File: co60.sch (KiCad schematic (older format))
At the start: 23 parts, among them J1 Conn_01x06, Q1 PZT2222A, SW1 SW_Push, U1 ATMEGA32U4, Y1 16MHz

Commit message: Add: Part numbers to top level schematic
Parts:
- C1, C2: Product (none) -> 06035A220JAT2A
- C3, C8: Product (none) -> CGB3B3JB1C105K055AB
- C4, C5, C6, C7: Product (none) -> C1608X8R1E104K080AA
- F1: Product (none) -> 0805L050WR
- RC1: Product (none) -> RC0603JR-071K5L
- R_MCU_3, R_MCU_4: Product (none) -> ERJ-3GEYJ103V
- R_USB_1, R_USB_2: Product (none) -> RC0603JR-0722RL
- R_USB_3, R_USB_4: Product (none) -> RMCF0603JT5K10
- SW1: DigiKey Page (none) -> https://www.digikey.ca/product-detail/en/e-switch/TL3342F16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; Product (none) -> TL3342F160QG/TR
- Y1: Product (none) -> NX2520SA-16MHZ-STD-CSW-4
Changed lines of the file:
@@
 F 1 "22p" H 7030 3280 30  0000 L CNN
 F 2 "Capacitors_SMD:C_0603" H 7043 3230 50  0001 C CNN
-F 3 "" H 7005 3380 50  0001 C CNN
+F 3 "http://datasheets.avx.com/C0GNP0-Dielectric.pdf" H 7005 3380 50  0001 C CNN
+F 4 "06035A220JAT2A" H 7005 3380 60  0001 C CNN "Product"
 	1    7005 3380
 	1    0    0    -1
@@
 F 1 "22p" H 6480 3280 30  0000 L CNN
 F 2 "Capacitors_SMD:C_0603" H 6493 3230 50  0001 C CNN
-F 3 "" H 6455 3380 50  0001 C CNN
+F 3 "http://datasheets.avx.com/C0GNP0-Dielectric.pdf" H 6455 3380 50  0001 C CNN
+F 4 "06035A220JAT2A" H 6455 3380 60  0001 C CNN "Product"
 	1    6455 3380
 	1    0    0    -1
@@
 F 1 "1u" H 6700 5605 50  0000 L CNN
 F 2 "Capacitors_SMD:C_0603" H 6713 5555 50  0001 C CNN
-F 3 "" H 6675 5705 50  0001 C CNN
+F 3 "https://product.tdk.com/info/en/catalog/datasheets/mlcc_commercial_lowprofile_en.pdf" H 6675 5705 50  0001 C CNN
+F 4 "CGB3B3JB1C105K055AB" H 6675 5705 60  0001 C CNN "Product"
 	1    6675 5705
 	1    0    0    -1
@@
 F 1 "100n" H 1175 950 50  0000 L CNN
 F 2 "Capacitors_SMD:C_0603" H 1188 900 50  0001 C CNN
-F 3 "" H 1150 1050 50  0001 C CNN
+F 3 "https://product.tdk.com/info/en/catalog/datasheets/mlcc_commercial_hightemp_en.pdf" H 1150 1050 50  0001 C CNN
+F 4 "C1608X8R1E104K080AA" H 1150 1050 60  0001 C CNN "Product"
 	1    1150 1050
 	1    0    0    -1
@@
 F 1 "100n" H 1425 950 50  0000 L CNN
 F 2 "Capacitors_SMD:C_0603" H 1438 900 50  0001 C CNN
-F 3 "" H 1400 1050 50  0001 C CNN
+F 3 "https://product.tdk.com/info/en/catalog/datasheets/mlcc_commercial_hightemp_en.pdf" H 1400 1050 50  0001 C CNN
+F 4 "C1608X8R1E104K080AA" H 1400 1050 60  0001 C CNN "Product"
 	1    1400 1050
 	1    0    0    -1
@@
 F 1 "100n" H 1675 950 50  0000 L CNN
 F 2 "Capacitors_SMD:C_0603" H 1688 900 50  0001 C CNN
-F 3 "" H 1650 1050 50  0001 C CNN
+F 3 "https://product.tdk.com/info/en/catalog/datasheets/mlcc_commercial_hightemp_en.pdf" H 1650 1050 50  0001 C CNN
+F 4 "C1608X8R1E104K080AA" H 1650 1050 60  0001 C CNN "Product"
 	1    1650 1050
 	1    0    0    -1
@@
 F 1 "100n" H 1925 950 50  0000 L CNN
 F 2 "Capacitors_SMD:C_0603" H 1938 900 50  0001 C CNN
-F 3 "" H 1900 1050 50  0001 C CNN
+F 3 "https://product.tdk.com/info/en/catalog/datasheets/mlcc_commercial_hightemp_en.pdf" H 1900 1050 50  0001 C CNN
+F 4 "C1608X8R1E104K080AA" H 1900 1050 60  0001 C CNN "Product"
 	1    1900 1050
 	1    0    0    -1
@@
 F 1 "1u" H 925 950 50  0000 L CNN
 F 2 "Capacitors_SMD:C_0603" H 938 900 50  0001 C CNN
-F 3 "" H 900 1050 50  0001 C CNN
+F 3 "https://product.tdk.com/info/en/catalog/datasheets/mlcc_commercial_lowprofile_en.pdf" H 900 1050 50  0001 C CNN
+F 4 "CGB3B3JB1C105K055AB" H 900 1050 60  0001 C CNN "Product"
 	1    900  1050
 	1    0    0    -1
@@
 F 2 "Resistors_SMD:R_0603" V 9695 4905 50  0001 C CNN
 F 3 "" H 9765 4905 50  0001 C CNN
+F 4 "ERJ-3GEYJ103V" V 9765 4905 60  0001 C CNN "Product"
 	1    9765 4905
 	1    0    0    -1
@@
 F 2 "Resistors_SMD:R_0603" V 4440 3605 50  0001 C CNN
 F 3 "" H 4510 3605 50  0001 C CNN
+F 4 "RC0603JR-0722RL" V 4510 3605 60  0001 C CNN "Product"
 	1    4510 3605
 	0    1    1    0
@@
 F 2 "Resistors_SMD:R_0603" V 4440 3780 50  0001 C CNN
 F 3 "" H 4510 3780 50  0001 C CNN
+F 4 "RC0603JR-0722RL" V 4510 3780 60  0001 C CNN "Product"
 	1    4510 3780
 	0    1    1    0
@@
 F 2 "Resistors_SMD:R_0603" V 3265 3245 50  0001 C CNN
 F 3 "" H 3335 3245 50  0001 C CNN
+F 4 "RMCF0603JT5K10" V 3335 3245 60  0001 C CNN "Product"
 	1    3335 3245
 	0    1    1    0
@@
 F 2 "Resistors_SMD:R_0603" V 3240 3415 50  0001 C CNN
 F 3 "" H 3310 3415 50  0001 C CNN
+F 4 "RMCF0603JT5K10" V 3310 3415 60  0001 C CNN "Product"
 	1    3310 3415
 	0    1    1    0
@@
 F 2 "Resistors_SMD:R_0603" V 6945 1915 50  0001 C CNN
 F 3 "" H 7015 1915 50  0001 C CNN
+F 4 "ERJ-3GEYJ103V" V 7015 1915 60  0001 C CNN "Product"
 	1    7015 1915
 	1    0    0    -1
@@
 F 1 "SW_Push" H 6685 2170 50  0000 C CNN
 F 2 "Buttons_Switches_SMD:SW_SPST_TL3342" H 6685 2430 50  0001 C CNN
-F 3 "" H 6685 2430 50  0001 C CNN
+F 3 "https://www.e-switch.com/system/asset/product_line/data_sheet/165/TL3342.pdf" H 6685 2430 50  0001 C CNN
+F 4 "TL3342F160QG/TR" H 6685 2230 60  0001 C CNN "Product"
+F 5 "https://www.digikey.ca/product-detail/en/e-switch/TL3342F160QG-TR/EG2531CT-ND/379004" H 6685 2230 60  0001 C CNN "DigiKey Page"
 	1    6685 2230
 	1    0    0    -1
@@
 F 2 "Resistors_SMD:R_0603" H 4365 1080 50  0001 C CNN
 F 3 "" H 4365 1080 50  0001 C CNN
+F 4 "RC0603JR-071K5L" H 4365 1080 60  0001 C CNN "Product"
 	1    4365 1080
 	0    1    1    0
@@
 F 2 "Crystals:Crystal_SMD_2520-4pin_2.5x2.0mm" H 6755 3030 50  0001 C CNN
 F 3 "https://www.digikey.com/product-detail/en/ndk-america-inc/NX2520SA-16MHZ-STD-CSW-4/644-1168-1-ND/3125557" H 6755 3030 50  0001 C CNN
+F 4 "NX2520SA-16MHZ-STD-CSW-4" H 6755 3030 60  0001 C CNN "Product"
 	1    6755 3030
 	-1   0    0    1
@@
 F 1 "500mA" V 3485 2850 50  0000 C CNN
 F 2 "Resistors_SMD:R_0805" H 3460 2650 50  0001 L CNN
-F 3 "" H 3410 2850 50  0001 C CNN
+F 3 "http://www.littelfuse.com/~/media/electronics/datasheets/resettable_ptcs/littelfuse_ptc_0805l_datasheet.pdf.pdf" H 3410 2850 50  0001 C CNN
+F 4 "0805L050WR" V 3410 2850 60  0001 C CNN "Product"
 	1    3410 2850
 	0    1    1    0

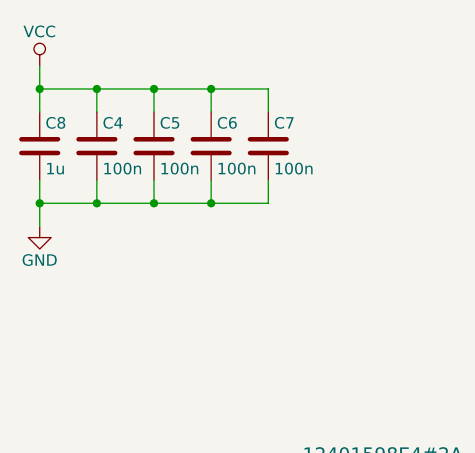
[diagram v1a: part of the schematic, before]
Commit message: Update: More component placement on PCB
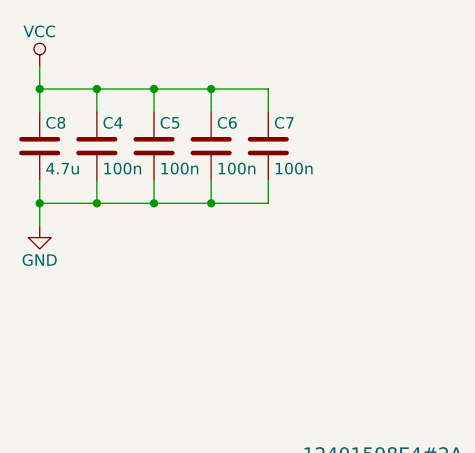
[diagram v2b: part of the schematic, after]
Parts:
- C8: value 1u -> 4.7u; Product CGB3B3JB1C105K055AB -> CL10A475KA8NQNC
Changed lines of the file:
@@
 P 900 1050
 F 0 "C8" H 925 1150 50  0000 L CNN
-F 1 "1u" H 925 950 50  0000 L CNN
+F 1 "4.7u" H 925 950 50  0000 L CNN
 F 2 "Capacitors_SMD:C_0603" H 938 900 50  0001 C CNN
-F 3 "https://product.tdk.com/info/en/catalog/datasheets/mlcc_commercial_lowprofile_en.pdf" H 900 1050 50  0001 C CNN
-F 4 "CGB3B3JB1C105K055AB" H 900 1050 60  0001 C CNN "Product"
+F 3 "http://www.samsungsem.com/kr/support/product-search/mlcc/__icsFiles/afieldfile/2016/12/21/CL10A475KA8NQNC_161221.pdf" H 900 1050 50  0001 C CNN
+F 4 "CL10A475KA8NQNC" H 900 1050 60  0001 C CNN "Product"
 	1    900  1050
 	1    0    0    -1

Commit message: Update: Rename some components
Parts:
- renumbered R_MCU_3 to RC2, R_MCU_4 to RC3, R_USB_1 to RC4, R_USB_2 to RC5, R_USB_3 to RC6, R_USB_4 to RC7
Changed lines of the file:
@@
 $EndSheet
 $Comp
-L R R_MCU_3
+L R RC2
 U 1 1 5AAF0E91
 P 9765 4905
-F 0 "R_MCU_3" V 9845 4905 50  0000 C CNN
+F 0 "RC2" V 9845 4905 50  0000 C CNN
 F 1 "10k" V 9765 4905 50  0000 C CNN
 F 2 "Resistors_SMD:R_0603" V 9695 4905 50  0001 C CNN
@@
 $EndComp
 $Comp
-L R R_USB_1
+L R RC4
 U 1 1 5ABDC854
 P 4510 3605
-F 0 "R_USB_1" V 4590 3605 50  0000 C CNN
+F 0 "RC4" V 4590 3605 50  0000 C CNN
 F 1 "22" V 4510 3605 50  0000 C CNN
 F 2 "Resistors_SMD:R_0603" V 4440 3605 50  0001 C CNN
@@
 $EndComp
 $Comp
-L R R_USB_2
+L R RC5
 U 1 1 5ABDCDB5
 P 4510 3780
-F 0 "R_USB_2" V 4590 3780 50  0000 C CNN
+F 0 "RC5" V 4590 3780 50  0000 C CNN
 F 1 "22" V 4510 3780 50  0000 C CNN
 F 2 "Resistors_SMD:R_0603" V 4440 3780 50  0001 C CNN
@@
 $EndComp
 $Comp
-L R R_USB_3
+L R RC6
 U 1 1 5ABE0CFC
 P 3335 3245
-F 0 "R_USB_3" V 3415 3245 50  0000 C CNN
+F 0 "RC6" V 3415 3245 50  0000 C CNN
 F 1 "5.1k" V 3335 3245 50  0000 C CNN
 F 2 "Resistors_SMD:R_0603" V 3265 3245 50  0001 C CNN
@@
 $EndComp
 $Comp
-L R R_USB_4
+L R RC7
 U 1 1 5ABE0F63
 P 3310 3415
-F 0 "R_USB_4" V 3390 3415 50  0000 C CNN
+F 0 "RC7" V 3390 3415 50  0000 C CNN
 F 1 "5.1k" V 3310 3415 50  0000 C CNN
 F 2 "Resistors_SMD:R_0603" V 3240 3415 50  0001 C CNN
@@
 $EndComp
 $Comp
-L R R_MCU_4
+L R RC3
 U 1 1 5ABF0E8F
 P 7015 1915
-F 0 "R_MCU_4" V 7095 1915 50  0000 C CNN
+F 0 "RC3" V 7095 1915 50  0000 C CNN
 F 1 "10k" V 7015 1915 50  0000 C CNN
 F 2 "Resistors_SMD:R_0603" V 6945 1915 50  0001 C CNN

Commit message: Update: Switch transistor to something smaller
I don't think I needed a transistor as big as I had for the
LEDs. I've switched to a SOT-23 footprint BJT that can
dissipate 500 mW. This should be more than enough for
68 LEDs at 5 mA each.
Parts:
- removed Q1: PZT2222A, TO_SOT_Packages_SMD:SOT-223, symbol PZT2222A
- added Q1: FMMT493TA, digikey-footprints:SOT-23-3, symbol FMMT493TA

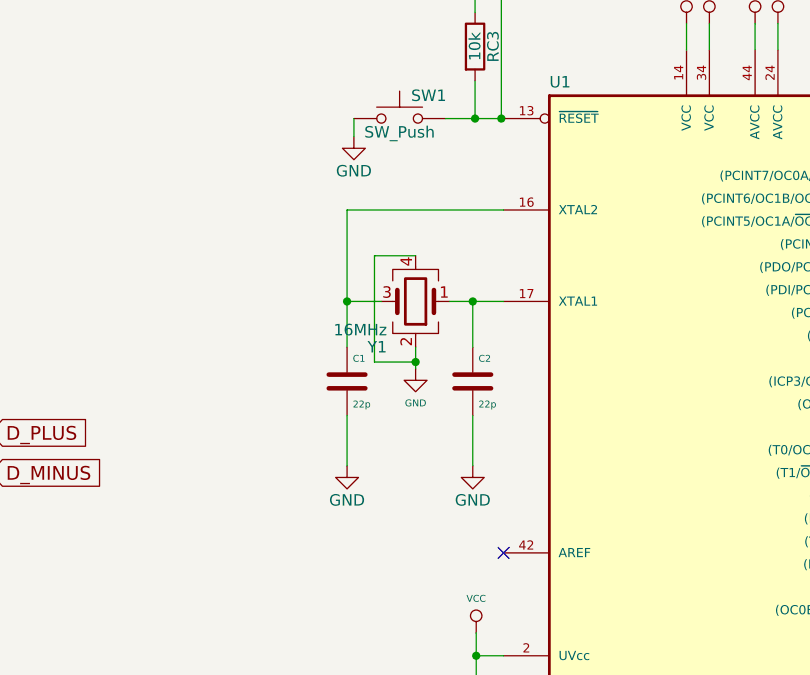
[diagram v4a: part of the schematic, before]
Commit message: Update: Reverse crystal connections
I'm not sure if this matters or not, but it seems
consistent with the way the GH60 does it.
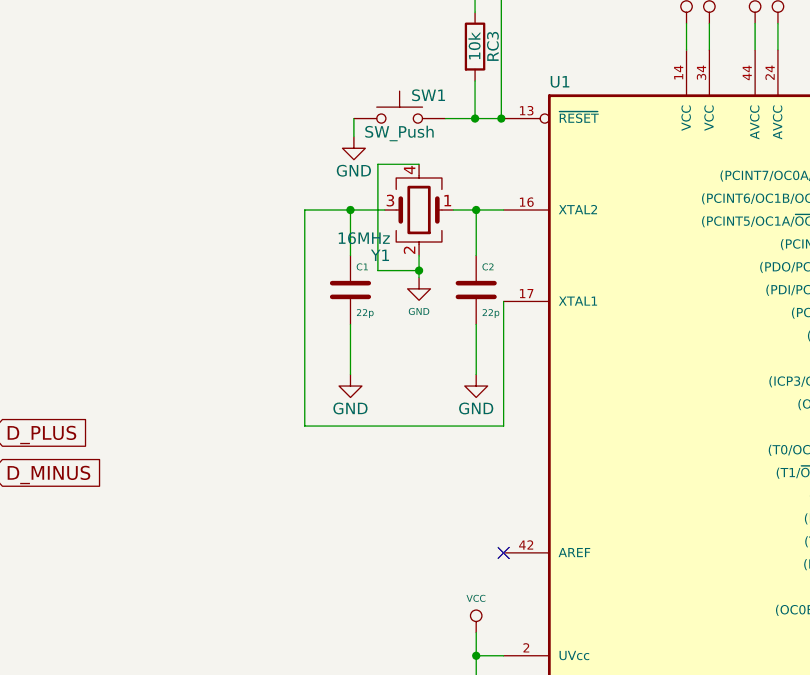
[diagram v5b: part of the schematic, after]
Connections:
- net at C1.1, Y1.3: now also U1.17 (XTAL1); no longer U1.16 (XTAL2)
- net at C2.1, Y1.1: now also U1.16 (XTAL2); no longer U1.17 (XTAL1)
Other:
- moved on the sheet: C1, C2, Y1
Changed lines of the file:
@@
 L C C2
 U 1 1 5AAB499C
-P 7005 3380
-F 0 "C2" H 7030 3480 30  0000 L CNN
-F 1 "22p" H 7030 3280 30  0000 L CNN
-F 2 "Capacitors_SMD:C_0603" H 7043 3230 50  0001 C CNN
-F 3 "http://datasheets.avx.com/C0GNP0-Dielectric.pdf" H 7005 3380 50  0001 C CNN
-F 4 "06035A220JAT2A" H 7005 3380 60  0001 C CNN "Product"
-	1    7005 3380
+P 7020 2980
+F 0 "C2" H 7045 3080 30  0000 L CNN
+F 1 "22p" H 7045 2880 30  0000 L CNN
+F 2 "Capacitors_SMD:C_0603" H 7058 2830 50  0001 C CNN
+F 3 "http://datasheets.avx.com/C0GNP0-Dielectric.pdf" H 7020 2980 50  0001 C CNN
+F 4 "06035A220JAT2A" H 7020 2980 60  0001 C CNN "Product"
+	1    7020 2980
 	1    0    0    -1
 $EndComp
@@
 L GND #PWR01
 U 1 1 5AAB4B68
-P 7005 3750
-F 0 "#PWR01" H 7005 3500 50  0001 C CNN
-F 1 "GND" H 7005 3600 50  0000 C CNN
-F 2 "" H 7005 3750 50  0001 C CNN
-F 3 "" H 7005 3750 50  0001 C CNN
-	1    7005 3750
+P 7020 3350
+F 0 "#PWR01" H 7020 3100 50  0001 C CNN
+F 1 "GND" H 7020 3200 50  0000 C CNN
+F 2 "" H 7020 3350 50  0001 C CNN
+F 3 "" H 7020 3350 50  0001 C CNN
+	1    7020 3350
 	1    0    0    -1
 $EndComp
@@
 L GND #PWR02
 U 1 1 5AAB4B9D
-P 6455 3750
-F 0 "#PWR02" H 6455 3500 50  0001 C CNN
-F 1 "GND" H 6455 3600 50  0000 C CNN
-F 2 "" H 6455 3750 50  0001 C CNN
-F 3 "" H 6455 3750 50  0001 C CNN
-	1    6455 3750
+P 6470 3350
+F 0 "#PWR02" H 6470 3100 50  0001 C CNN
+F 1 "GND" H 6470 3200 50  0000 C CNN
+F 2 "" H 6470 3350 50  0001 C CNN
+F 3 "" H 6470 3350 50  0001 C CNN
+	1    6470 3350
 	1    0    0    -1
 $EndComp
@@
 L C C1
 U 1 1 5AAB494D
-P 6455 3380
-F 0 "C1" H 6480 3480 30  0000 L CNN
-F 1 "22p" H 6480 3280 30  0000 L CNN
-F 2 "Capacitors_SMD:C_0603" H 6493 3230 50  0001 C CNN
-F 3 "http://datasheets.avx.com/C0GNP0-Dielectric.pdf" H 6455 3380 50  0001 C CNN
-F 4 "06035A220JAT2A" H 6455 3380 60  0001 C CNN "Product"
-	1    6455 3380
+P 6470 2980
+F 0 "C1" H 6495 3080 30  0000 L CNN
+F 1 "22p" H 6495 2880 30  0000 L CNN
+F 2 "Capacitors_SMD:C_0603" H 6508 2830 50  0001 C CNN
+F 3 "http://datasheets.avx.com/C0GNP0-Dielectric.pdf" H 6470 2980 50  0001 C CNN
+F 4 "06035A220JAT2A" H 6470 2980 60  0001 C CNN "Product"
+	1    6470 2980
 	1    0    0    -1
 $EndComp
@@
 L GND #PWR06
 U 1 1 5B375186
-P 6755 3325
-F 0 "#PWR06" H 6755 3075 50  0001 C CNN
-F 1 "GND" H 6755 3175 30  0000 C CNN
-F 2 "" H 6755 3325 50  0001 C CNN
-F 3 "" H 6755 3325 50  0001 C CNN
-	1    6755 3325
+P 6770 2925
+F 0 "#PWR06" H 6770 2675 50  0001 C CNN
+F 1 "GND" H 6770 2775 30  0000 C CNN
+F 2 "" H 6770 2925 50  0001 C CNN
+F 3 "" H 6770 2925 50  0001 C CNN
+	1    6770 2925
 	1    0    0    -1
 $EndComp
@@
 L Crystal_GND24 Y1
 U 1 1 5ADF9892
-P 6755 3030
-F 0 "Y1" H 6880 3230 50  0000 L CNN
-F 1 "16MHz" H 6880 3155 50  0000 L CNN
-F 2 "Crystals:Crystal_SMD_2520-4pin_2.5x2.0mm" H 6755 3030 50  0001 C CNN
-F 3 "https://www.digikey.com/product-detail/en/ndk-america-inc/NX2520SA-16MHZ-STD-CSW-4/644-1168-1-ND/3125557" H 6755 3030 50  0001 C CNN
-F 4 "NX2520SA-16MHZ-STD-CSW-4" H 6755 3030 60  0001 C CNN "Product"
-	1    6755 3030
+P 6770 2630
+F 0 "Y1" H 6895 2830 50  0000 L CNN
+F 1 "16MHz" H 6895 2755 50  0000 L CNN
+F 2 "Crystals:Crystal_SMD_2520-4pin_2.5x2.0mm" H 6770 2630 50  0001 C CNN
+F 3 "https://www.digikey.com/product-detail/en/ndk-america-inc/NX2520SA-16MHZ-STD-CSW-4/644-1168-1-ND/3125557" H 6770 2630 50  0001 C CNN
+F 4 "NX2520SA-16MHZ-STD-CSW-4" H 6770 2630 60  0001 C CNN "Product"
+	1    6770 2630
 	-1   0    0    1
 $EndComp
@@
 Wire Wire Line
 	3985 4420 3855 4420
-Connection ~ 7005 3030
-Wire Wire Line
-	7005 3230 7005 3030
-Connection ~ 6755 3295
-Wire Wire Line
-	6575 3295 6755 3295
-Wire Wire Line
-	6575 2830 6575 3295
-Wire Wire Line
-	6755 2830 6575 2830
-Wire Wire Line
-	6755 3230 6755 3325
-Wire Wire Line
-	6605 3030 6455 3030
-Wire Wire Line
-	7140 3030 6905 3030
+Connection ~ 7020 2630
+Wire Wire Line
+	7020 2830 7020 2630
+Connection ~ 6770 2895
+Wire Wire Line
+	6590 2895 6770 2895
+Wire Wire Line
+	6590 2430 6590 2895
+Wire Wire Line
+	6770 2430 6590 2430
+Wire Wire Line
+	6770 2830 6770 2925
+Wire Wire Line
+	6270 2630 6620 2630
 Wire Wire Line
 	9140 5380 9295 5380
@@
 	4895 3605 4660 3605
 Connection ~ 7015 2230
-Connection ~ 6455 3030
-Wire Wire Line
-	6455 2630 7140 2630
-Wire Wire Line
-	6455 2630 6455 3230
-Wire Wire Line
-	6455 3530 6455 3750
-Wire Wire Line
-	7005 3530 7005 3750
+Connection ~ 6470 2630
+Wire Wire Line
+	6470 3130 6470 3350
+Wire Wire Line
+	7020 3130 7020 3350
 Wire Wire Line
 	7015 1765 7015 1650
@@
 Wire Wire Line
 	5015 1380 5015 1485
+Wire Wire Line
+	6920 2630 7140 2630
+Wire Wire Line
+	6470 2630 6470 2830
+Wire Wire Line
+	6270 2630 6270 3575
+Wire Wire Line
+	6270 3575 7140 3575
+Wire Wire Line
+	7140 3575 7140 3030
 $EndSCHEMATC

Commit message: Update: More work on PCB routing
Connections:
- net D_MINUS renamed D_N
- net D_PLUS renamed D_P
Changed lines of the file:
@@
 $EndComp
 Text GLabel 4895 3605 2    60   Input ~ 0
-D_PLUS
+D_P
 Text GLabel 4895 3780 2    60   Input ~ 0
-D_MINUS
+D_N
 Text GLabel 6885 4880 0    60   Input ~ 0
-D_PLUS
+D_P
 Text GLabel 6885 4780 0    60   Input ~ 0
-D_MINUS
+D_N
 $Comp
 L Crystal_GND24 Y1

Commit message: Add: Fields for components that shouldn't be part of the BOM
This ensures that all of the switches won't be added as BOM
lines.
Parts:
- J1: Config (none) -> dnf
- U1: Description (none) -> Microcontroller
- USB1: Description (none) -> USB Type-C connector
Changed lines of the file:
@@
 F 2 "tqfp:TQFP44" H 8640 1955 50  0001 C CNN
 F 3 "http://ww1.microchip.com/downloads/en/DeviceDoc/Atmel-7766-8-bit-AVR-ATmega16U4-32U4_Summary.pdf" H 8140 3930 60  0001 C CNN
+F 4 "Microcontroller" H 8140 3930 60  0001 C CNN "Description"
 	1    8140 3930
 	1    0    0    -1
@@
 F 2 "Socket_Strips:Socket_Strip_Straight_1x06_Pitch2.54mm" H 10595 2915 50  0001 C CNN
 F 3 "" H 10595 2915 50  0001 C CNN
+F 4 "dnf" H 10595 2915 60  0001 C CNN "Config"
 	1    10595 2915
 	1    0    0    -1
@@
 F 2 "Type-C:12401598E4#2A" H 1700 3450 60  0001 C CNN
 F 3 "https://media.digikey.com/pdf/Data%20Sheets/Amphenol%20PDFs/12401598E4%232A_Dwg.pdf" H 1700 3450 60  0001 C CNN
+F 4 "USB Type-C connector" H 2400 3400 60  0001 C CNN "Description"
 	1    2400 3400
 	1    0    0    -1

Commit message: Update: Work on BOM
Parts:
- DP1: Description (none) -> Rail-to-rail ESD protection circuitry
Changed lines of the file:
@@
 F 2 "locallib:SOT143B" H 4335 4270 50  0001 C CNN
 F 3 "https://assets.nexperia.com/documents/data-sheet/PRTR5V0U2X.pdf" H 4335 4270 50  0001 C CNN
+F 4 "Rail-to-rail ESD protection circuitry" H 4285 4320 60  0001 C CNN "Description"
 	1    4285 4320
 	1    0    0    -1
